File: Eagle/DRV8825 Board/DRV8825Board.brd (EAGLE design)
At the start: 65 x 50 mm, 10 parts, among them X1 22-23-2031, X2 22-23-2041, X3 22-23-2041

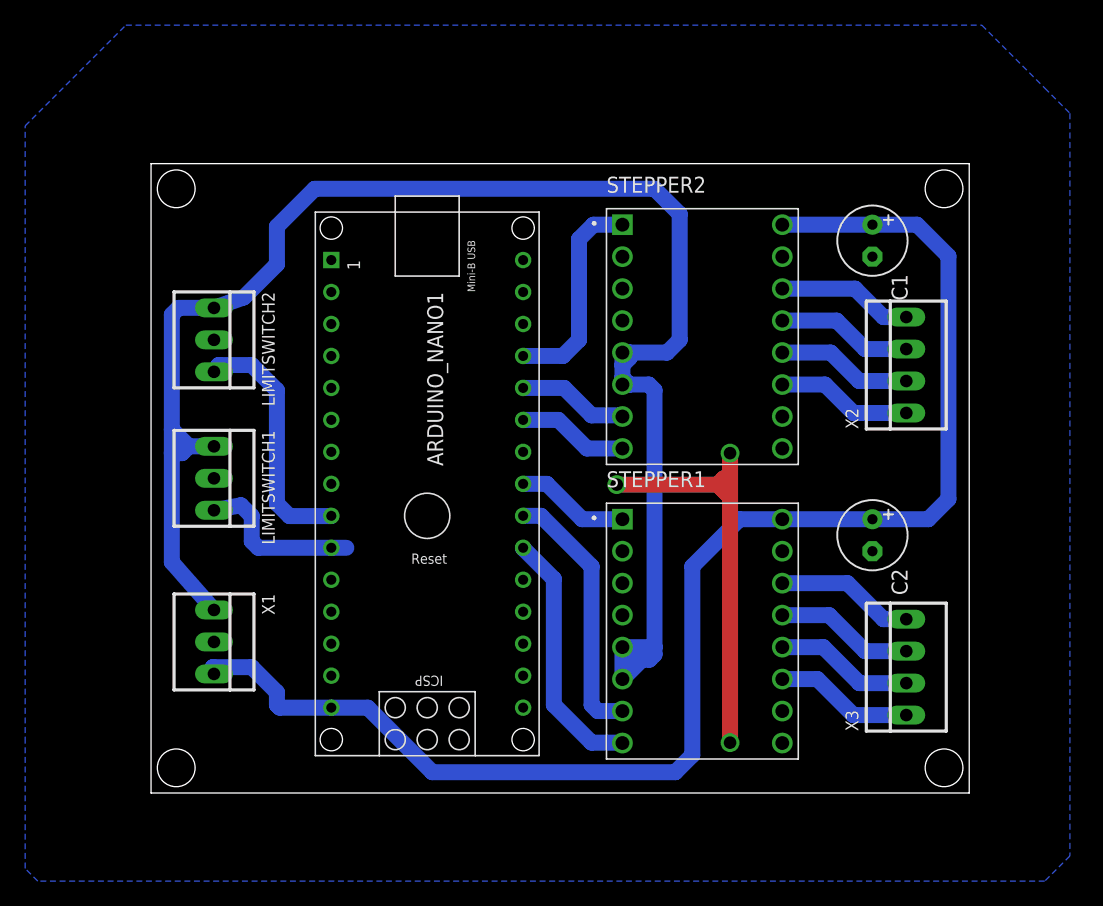
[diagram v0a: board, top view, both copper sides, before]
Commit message: Added a fan controller circuit
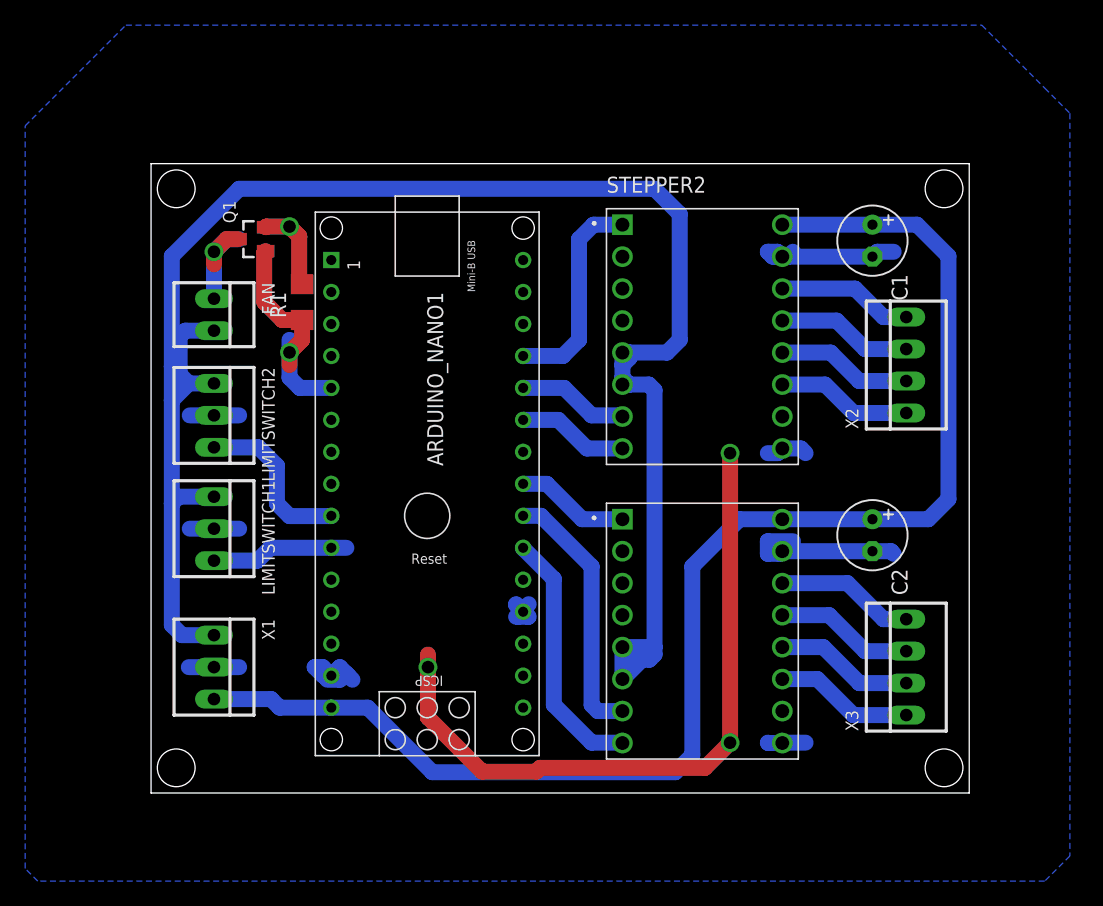
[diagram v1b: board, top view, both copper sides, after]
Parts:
- added FAN: 22-23-2021, con-molex:22-23-2021
- added Q1: FDV305N, FDV305N:SOT23
- added R1: 1k, rcl:R1206
- moved LIMITSWITCH2 6.00 mm to (5.00, 30.0)
- moved LIMITSWITCH1 4.00 mm to (5.00, 21.0)
- moved X1 2.00 mm to (5.00, 10.0)
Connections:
- new net FANOUT: ARDUINO_NANO1.5, Q1.1, R1.1
- new net N$1: FAN.1, Q1.3
- net 5V: now also FAN.2
- net GND: now also Q1.2, R1.2
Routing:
- net GND: track 34.8 -> 117.8 mm, vias 3 -> 4
- net FANOUT: track 0.00 -> 18.3 mm, vias 0 -> 1
- net 5V: track 134.0 -> 146.5 mm
- net N$1: track 0.00 -> 9.46 mm, vias 0 -> 1
- net SGN2: track 19.9 -> 13.3 mm
- net 12V: track 114.3 -> 112.1 mm
- net SGN: track 13.1 -> 10.9 mm

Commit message: Updated to include all the limitswitches from the gripper
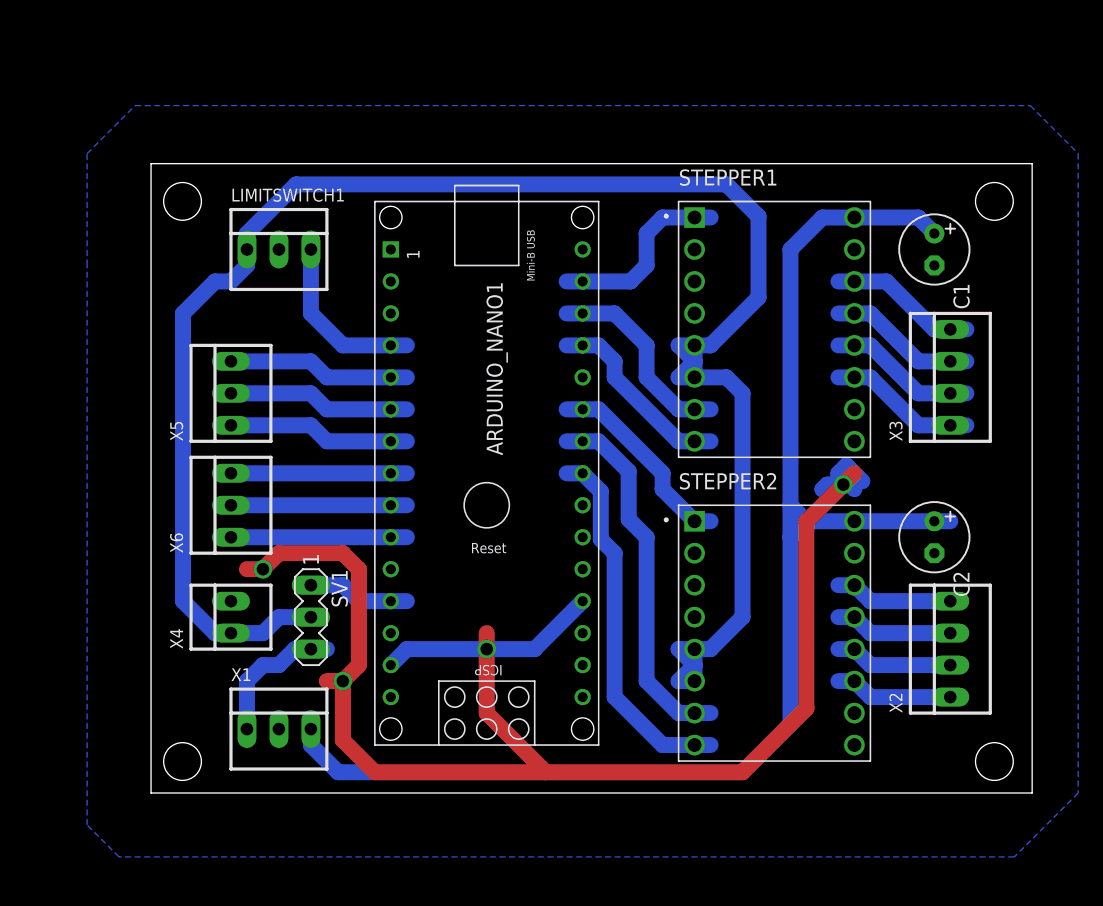
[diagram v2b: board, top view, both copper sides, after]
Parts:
- removed FAN: 22-23-2021, con-molex:22-23-2021
- removed LIMITSWITCH2: 22-23-2031, con-molex:22-23-2031
- removed Q1: FDV305N, FDV305N:SOT23
- removed R1: 1k, rcl:R1206
- added SV1: (no value), con-lstb:MA03-1
- added X4: 22-23-2021, con-molex:22-23-2021
- added X5, X6: 22-23-2031, con-molex:22-23-2031
- moved STEPPER1 24.6 mm to (49.5, 36.8)
- moved STEPPER2 24.2 mm to (49.5, 12.7)
- moved X3 23.3 mm to (63.5, 33.0)
- moved X2 22.8 mm to (63.5, 11.4)
- moved LIMITSWITCH1 22.8 mm to (10.2, 43.2), turned to 0 degrees
- moved X1 7.13 mm to (10.2, 5.08), turned to 0 degrees
- moved C1 4.97 mm to (62.2, 43.2)
- moved C2 4.92 mm to (62.2, 20.3)
- moved ARDUINO_NANO1 4.80 mm to (26.7, 22.9)
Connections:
- removed net FANOUT: ARDUINO_NANO1.5, Q1.1, R1.1
- removed net N$1: FAN.1, Q1.3
- new net SGN1: ARDUINO_NANO1.5, X5.3
- new net SGN3: ARDUINO_NANO1.7, X5.1
- new net SGN4: ARDUINO_NANO1.8, X6.3
- new net SGN5: ARDUINO_NANO1.9, X6.2
- new net SGN6: ARDUINO_NANO1.10, X6.1
- new net VIN: ARDUINO_NANO1.15
- net 12V: no longer ARDUINO_NANO1.15
- net 5V: now also SV1.1, SV1.2, SV1.3, X4.1; no longer FAN.2, LIMITSWITCH2.1
- net DIR1: now also ARDUINO_NANO1.27; no longer ARDUINO_NANO1.21
- net DIR2: now also ARDUINO_NANO1.23; no longer ARDUINO_NANO1.25
- net ENABLE1: now also ARDUINO_NANO1.29; no longer ARDUINO_NANO1.23
- net ENABLE2: now also ARDUINO_NANO1.25; no longer ARDUINO_NANO1.27
- net GND: now also X4.2; no longer LIMITSWITCH2.2, Q1.2, R1.2
- net SGN: now also ARDUINO_NANO1.4; no longer ARDUINO_NANO1.10
- net SGN2: now also ARDUINO_NANO1.6, X5.2; no longer ARDUINO_NANO1.9, LIMITSWITCH2.3
- net STEP1: now also ARDUINO_NANO1.28; no longer ARDUINO_NANO1.22
- net STEP2: now also ARDUINO_NANO1.24; no longer ARDUINO_NANO1.26
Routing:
- net STEP2: track 8.83 -> 29.3 mm
- net DIR2: track 8.83 -> 29.3 mm
- net FANOUT: track 18.3 -> 0.00 mm, vias 1 -> 0
- net 5V: track 146.5 -> 163.9 mm
- net SGN3: track 0.00 -> 14.5 mm
- net SGN1: track 0.00 -> 14.5 mm
- net SGN6: track 0.00 -> 14.0 mm
- net SGN5: track 0.00 -> 14.0 mm
- net SGN4: track 0.00 -> 14.0 mm
- net N$1: track 9.46 -> 0.00 mm, vias 1 -> 0
- net GND: track 117.8 -> 124.0 mm
- net ENABLE1: track 9.05 -> 15.0 mm
- net DIR1: track 20.2 -> 15.3 mm
- net STEP1: track 20.8 -> 16.1 mm
- net 12V: track 112.1 -> 107.6 mm
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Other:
- board size 65 x 50 mm -> 70 x 50 mm
